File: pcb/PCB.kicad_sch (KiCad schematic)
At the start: 35 parts, among them J1 Conn_01x15, J2 USB_C_Receptacle_USB2.0, J3 Conn_01x15, J4 TC2030, J5 Conn_01x04, SW1 SW_Push, SW2 SW_Push, U1 SN65HVD230, U2 AMS1117-3.3, U3 STM32F103C8T6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

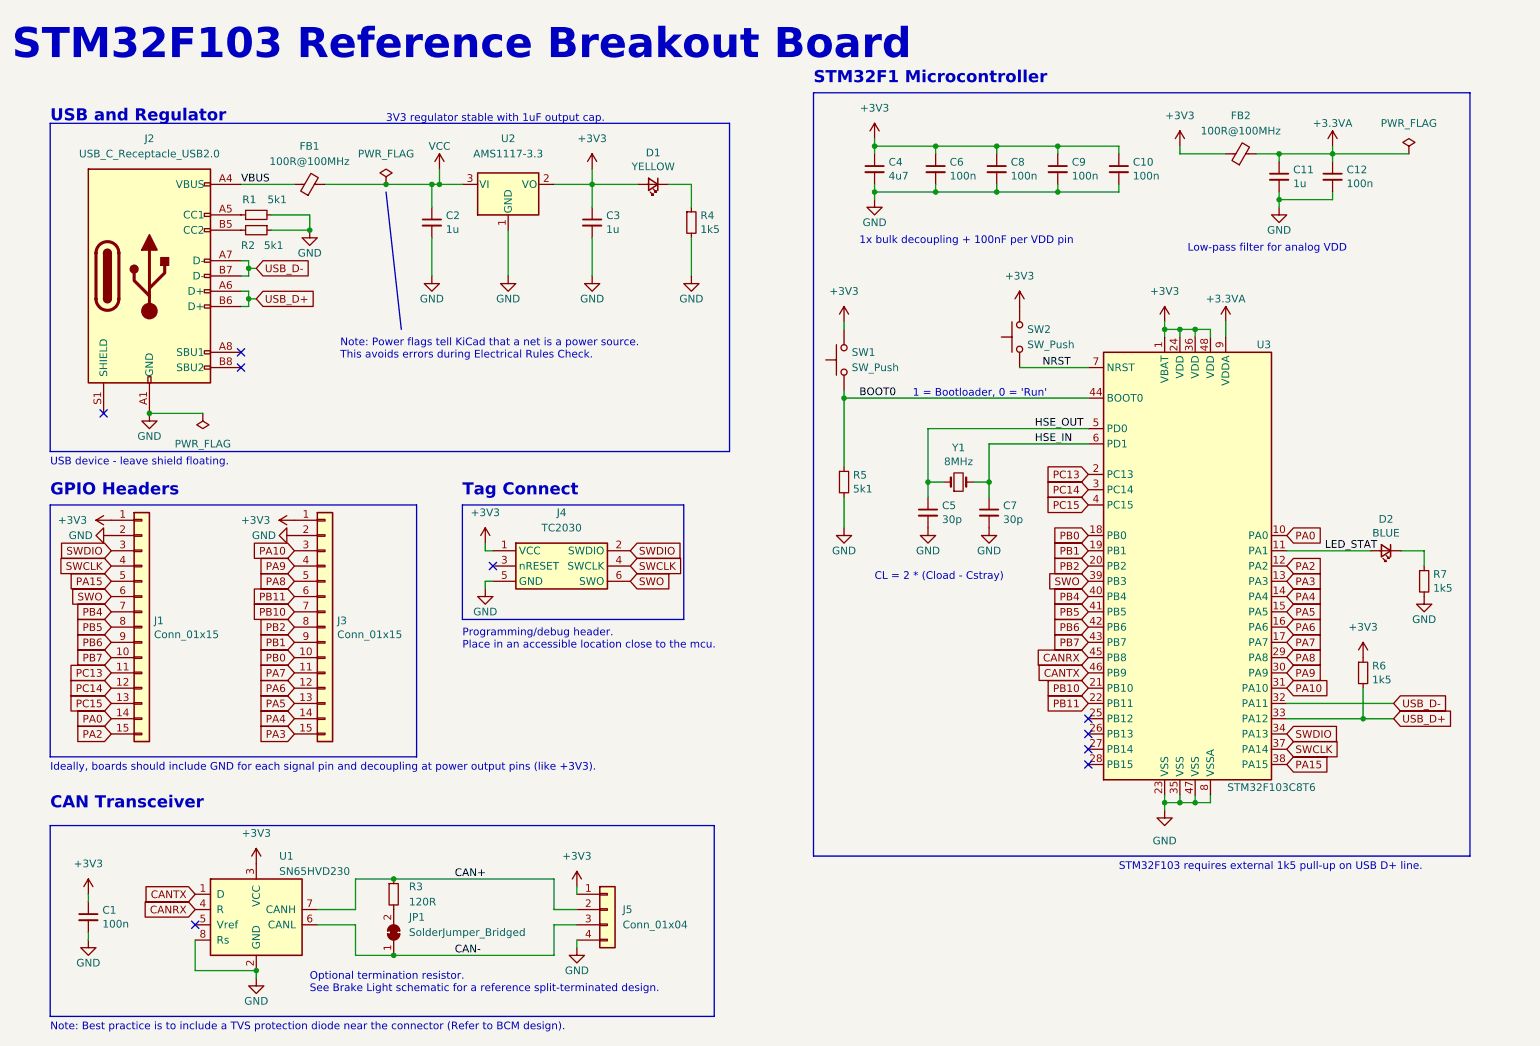
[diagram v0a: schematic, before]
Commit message: Use Neopixels for segment displays (#2)
* Create schematic

* Laid out and routed PCB

* fix github workflow path

* re-fix github workflow :(

* Added debug/test header

* Added silkscreen markings

* Fixed DRC violations

* Added 5v output on main connector, labeled 5v tolerant pins

* De-borked symbol library for segment displays

* Changes from design review

* Added firmware project structure and testing firmware

* Added part numbers for assembly

* Started work on discrete led displays

* PCB layout work

* Finished layout

* bottom text
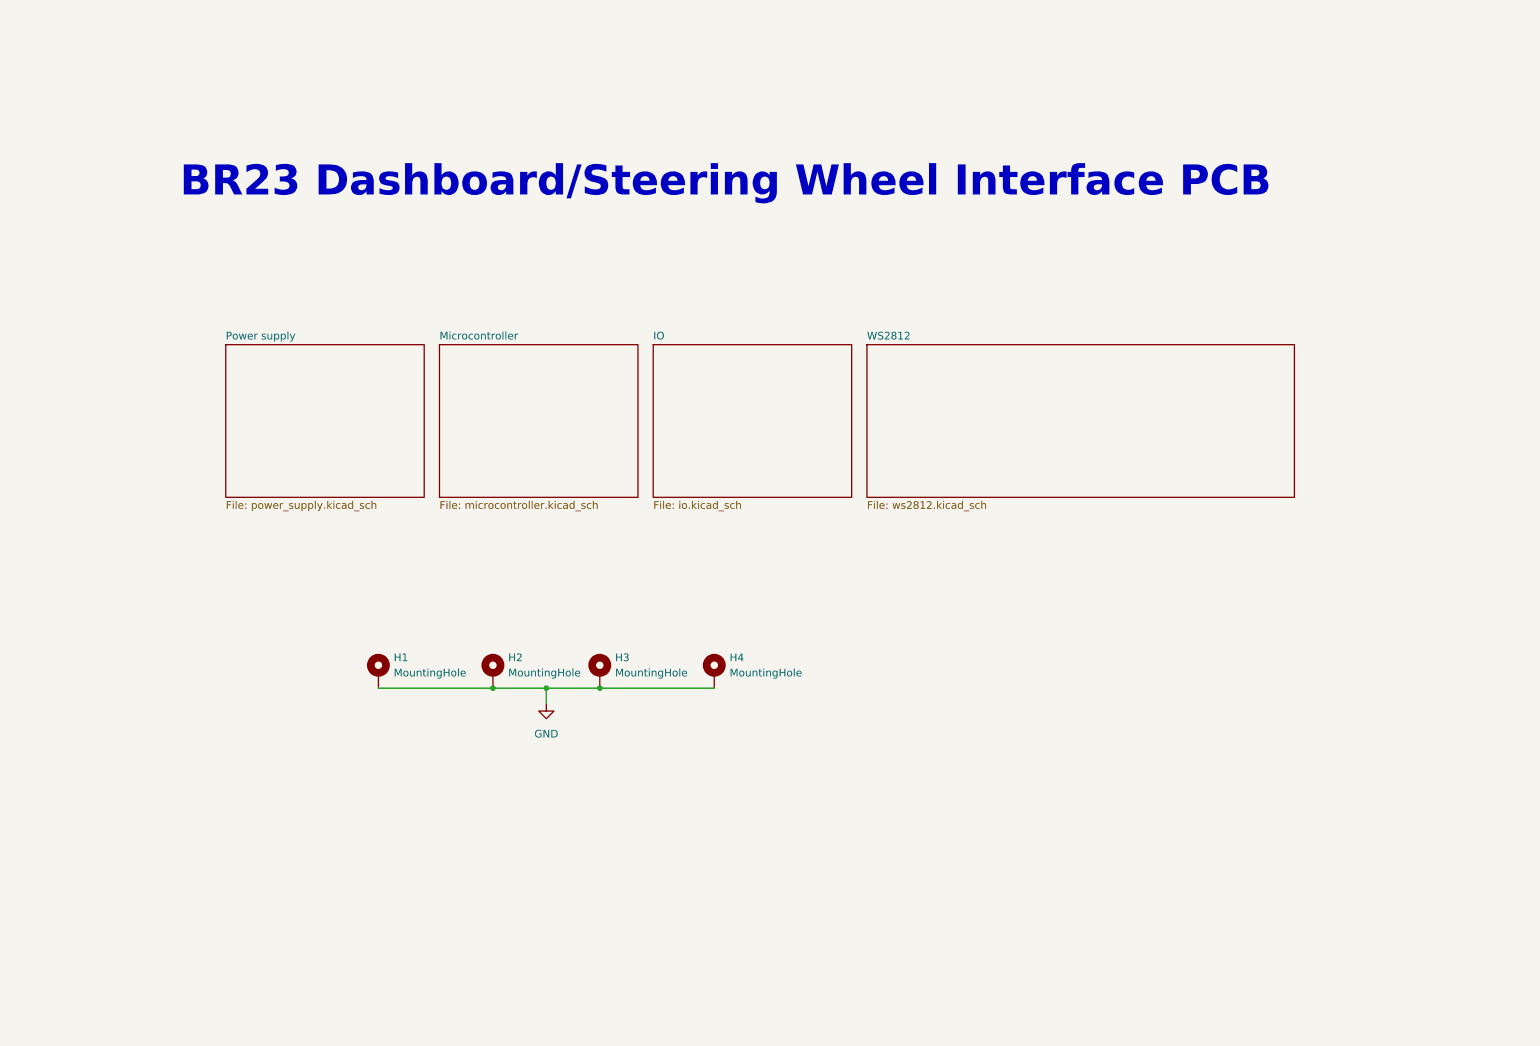
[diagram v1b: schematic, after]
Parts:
- removed C1, C10, C12, C6, C8, C9: 100n, Capacitor_SMD:C_0402_1005Metric, symbol Device:C_Small
- removed C11, C2, C3: 1u, Capacitor_SMD:C_0603_1608Metric, symbol Device:C_Small
- removed C4: 4u7, Capacitor_SMD:C_0603_1608Metric, symbol Device:C_Small
- removed C5, C7: 30p, Capacitor_SMD:C_0402_1005Metric, symbol Device:C_Small
- removed D1: YELLOW, LED_SMD:LED_0603_1608Metric, symbol Device:LED_Small
- removed D2: BLUE, LED_SMD:LED_0603_1608Metric, symbol Device:LED_Small
- removed FB1, FB2: 100R@100MHz, Resistor_SMD:R_0805_2012Metric, symbol Device:FerriteBead_Small
- removed J1, J3: Conn_01x15, Connector_PinHeader_2.54mm:PinHeader_1x15_P2.54mm_Vertical, symbol Connector_Generic:Conn_01x15
- removed J2: USB_C_Receptacle_USB2.0, Connector_USB:USB_C_Receptacle_HRO_TYPE-C-31-M-12, symbol Connector:USB_C_Receptacle_USB2.0
- removed J4: TC2030, Connector:Tag-Connect_TC2030-IDC-NL_2x03_P1.27mm_Vertical, symbol TC2030:TC2030
- removed J5: Conn_01x04, Connector_PinHeader_2.54mm:PinHeader_1x04_P2.54mm_Vertical, symbol Connector_Generic:Conn_01x04
- removed JP1: SolderJumper_Bridged, Jumper:SolderJumper-2_P1.3mm_Bridged_RoundedPad1.0x1.5mm, symbol Jumper:SolderJumper_2_Bridged
- removed R1, R2, R5: 5k1, Resistor_SMD:R_0402_1005Metric, symbol Device:R_Small
- removed R3: 120R, Resistor_SMD:R_0402_1005Metric, symbol Device:R_Small
- removed R4, R6, R7: 1k5, Resistor_SMD:R_0402_1005Metric, symbol Device:R_Small
- removed SW1, SW2: SW_Push, Button_Switch_SMD:SW_Push_1P1T_NO_CK_KSC7xxJ, symbol Switch:SW_Push
- removed U1: SN65HVD230, Package_SO:SOIC-8_3.9x4.9mm_P1.27mm, symbol Interface_CAN_LIN:SN65HVD230
- removed U2: AMS1117-3.3, Package_TO_SOT_SMD:SOT-223-3_TabPin2, symbol Regulator_Linear:AMS1117-3.3
- removed U3: STM32F103C8T6, Package_QFP:LQFP-48_7x7mm_P0.5mm, symbol MCU_ST_STM32F1:STM32F103C8Tx
- removed Y1: 8MHz, Crystal:Crystal_SMD_5032-2Pin_5.0x3.2mm, symbol Device:Crystal_Small
- added H1, H2, H3, H4: MountingHole, MountingHole:MountingHole_3.5mm_Pad, symbol Mechanical:MountingHole_Pad
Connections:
- net GND: now also H1.1, H2.1, H3.1, H4.1
- no-connect marks 9 -> 0
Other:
- added sheet IO (io.kicad_sch)
- added sheet Microcontroller (microcontroller.kicad_sch)
- added sheet Power supply (power_supply.kicad_sch)
- added sheet WS2812 (ws2812.kicad_sch)
- note added: "BR23 Dashboard/Steering Wheel Interface PCB"
- note removed: "1 = Bootloader, 0 = 'Run'"
- note removed: "1x bulk decoupling + 100nF per VDD pin"
- note removed: "3V3 regulator stable with 1uF output cap."
- note removed: "CAN Transceiver"
- note removed: "CL = 2 * (Cload - Cstray)"
- note removed: "GPIO Headers"
- note removed: "Ideally, boards should include GND for each signal pin and decoupling at power output pins (like +3V3)."
- note removed: "Low-pass filter for analog VDD"
- note removed: "Note: Best practice is to include a TVS protection diode near the connector (Refer to BCM design)."
- note removed: "Note: Power flags tell KiCad that a net is a power source. This avoids errors during Electrical Rules Check."
- note removed: "Optional termination resistor. See Brake Light schematic for a reference split-terminated design."
- note removed: "Programming/debug header. Place in an accessible location close to the mcu."
- note removed: "STM32F1 Microcontroller"
- note removed: "STM32F103 Reference Breakout Board"
- note removed: "STM32F103 requires external 1k5 pull-up on USB D+ line."
- note removed: "Tag Connect"
- note removed: "USB and Regulator"
- note removed: "USB device - leave shield floating."
- title: STM32F103 Reference Breakout Board -> BR23 Dashboard PCB
